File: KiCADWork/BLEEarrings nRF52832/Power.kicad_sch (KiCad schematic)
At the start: 17 parts, among them SW1 TK-6580B-1, U1 XB6096I2SV, U2 MCP73831T-2ACI/OT, U4 AP7361C-33FGE-7

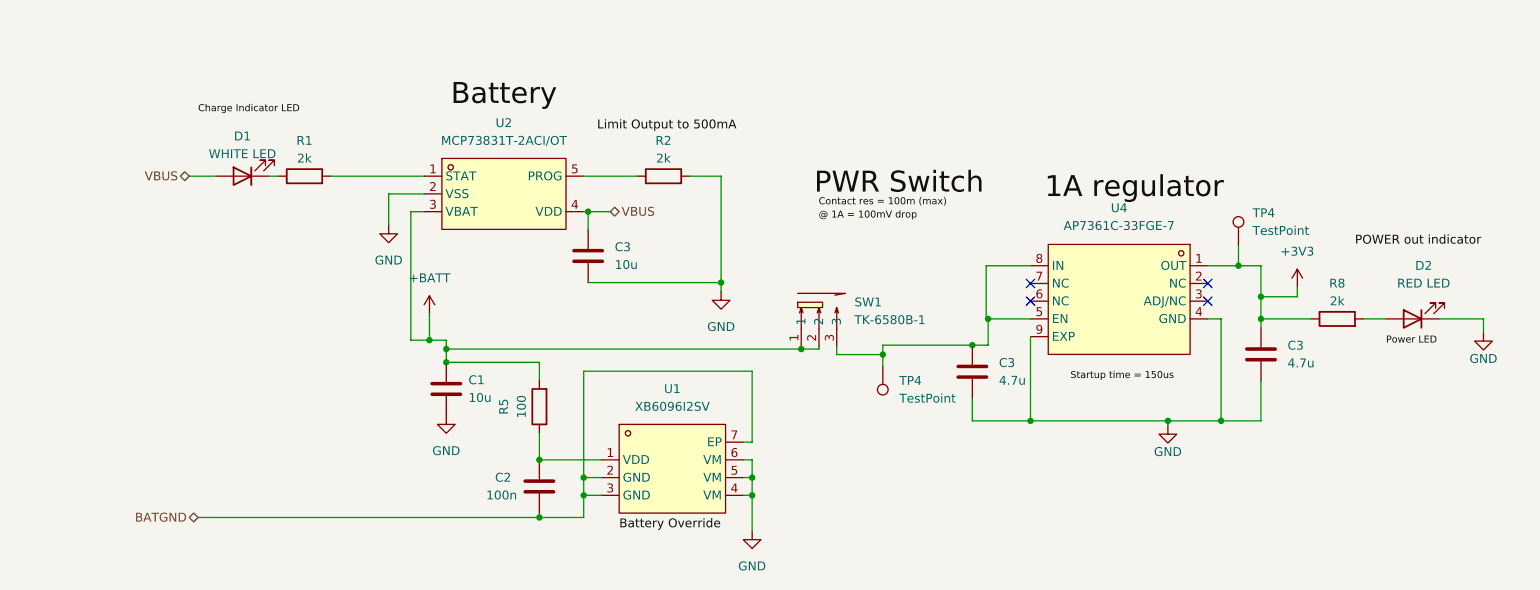
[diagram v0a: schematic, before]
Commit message: New Chip NRF52833
large changes
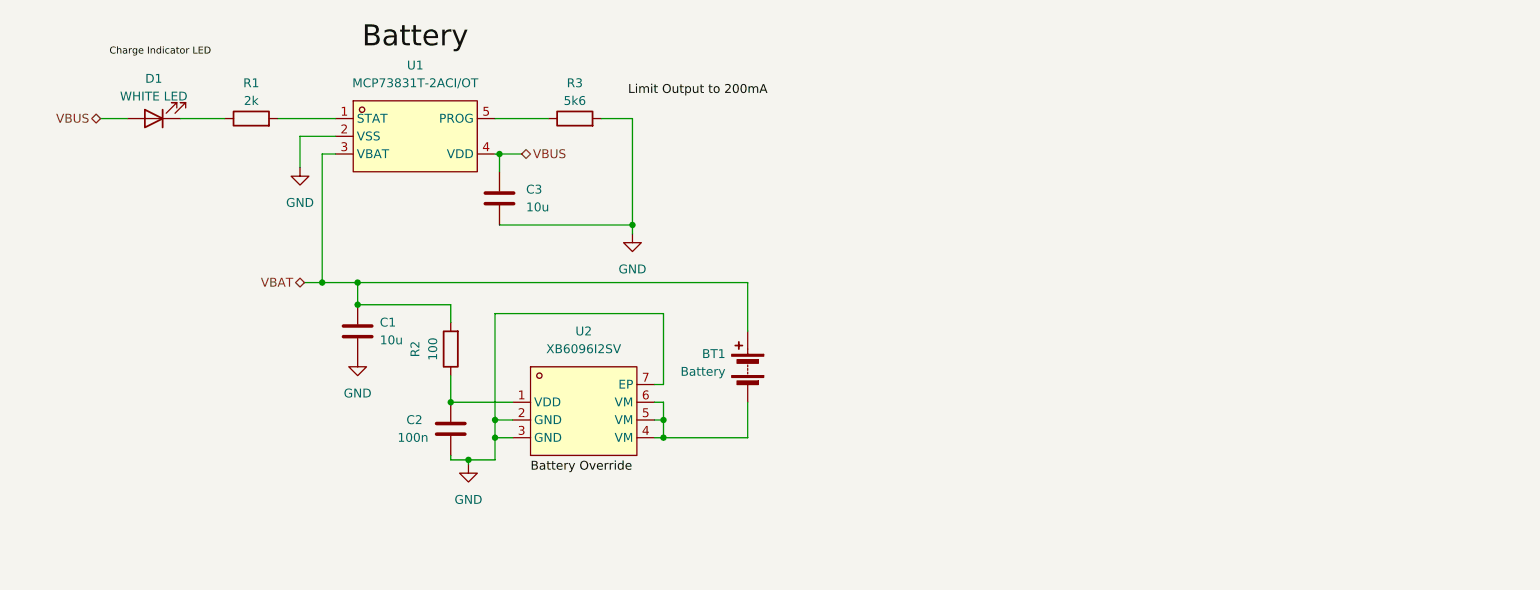
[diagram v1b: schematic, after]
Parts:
- removed C3 (x2): 4.7u, Capacitor_SMD:C_0402_1005Metric_Pad0.74x0.62mm_HandSolder, symbol Device:C
- removed C3: 10u, Capacitor_SMD:C_0402_1005Metric_Pad0.74x0.62mm_HandSolder, symbol Device:C
- removed D2: RED LED, LED_SMD:LED_0603_1608Metric_Pad1.05x0.95mm_HandSolder, symbol Device:LED
- removed R5: 100, Resistor_SMD:R_0402_1005Metric_Pad0.72x0.64mm_HandSolder, symbol Device:R
- removed R8: 2k, Resistor_SMD:R_0402_1005Metric_Pad0.72x0.64mm_HandSolder, symbol Device:R
- removed SW1: TK-6580B-1, easyeda2kicad:SW-TH_TK-6580B-1, symbol easyeda2kicad:TK-6580B-1
- removed TP4 (x2): TestPoint, TestPoint:TestPoint_Pad_D1.0mm, symbol Connector:TestPoint
- removed U1: XB6096I2SV, easyeda2kicad:WDFN-6_L2.0-W2.0-P0.65-BL-EP, symbol easyeda2kicad:XB6096I2SV
- removed U2: MCP73831T-2ACI/OT, easyeda2kicad:SOT-23-5_L3.0-W1.7-P0.95-LS2.8-BL, symbol easyeda2kicad:MCP73831T-2ACI_OT
- removed U4: AP7361C-33FGE-7, easyeda2kicad:DFN-8_L3.0-W3.0-P0.65-BL-EP, symbol easyeda2kicad:AP7361C-33FGE-7
- added BT1: Battery, easyeda2kicad:CONN-TH_1.25-2AW, symbol Device:Battery
- added C3: 10u, Capacitor_SMD:C_0402_1005Metric_Pad0.74x0.62mm_HandSolder, symbol Device:C
- added R3: 5k6, Resistor_SMD:R_0402_1005Metric_Pad0.72x0.64mm_HandSolder, symbol Device:R
- added U1: MCP73831T-2ACI/OT, easyeda2kicad:SOT-23-5_L3.0-W1.7-P0.95-LS2.8-BL, symbol easyeda2kicad:MCP73831T-2ACI_OT
- added U2: XB6096I2SV, easyeda2kicad:WDFN-6_L2.0-W2.0-P0.65-BL-EP, symbol easyeda2kicad:XB6096I2SV
- R2: value 2k -> 100
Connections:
- net BATGND is gone; now on net GND: C2.2
- net GND: now also C3.2, R3.2, U1.2 (VSS), U2.2 (GND), U2.3 (GND), U2.7 (EP); no longer R2.2
- net VBUS: now also C3.1, U1.4 (VDD)
- net at R2.1: now also C2.1, U2.1 (VDD)
- net at R1.2: now also U1.1 (STAT)
- net +BATT renamed VBAT
- net VBAT: now also R2.2, BT1.1 (+), U1.3 (VBAT)
- new net: R3.1, U1.5 (PROG)
- new net: BT1.2 (-), U2.4 (VM), U2.5 (VM), U2.6 (VM)
- no-connect marks 4 -> 0

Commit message: Dock Updates
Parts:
- R3: value 5k6 -> 4k99
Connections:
- net GND: now also U2.4 (VM), U2.5 (VM), U2.6 (VM); no longer U2.2 (GND), U2.3 (GND), U2.7 (EP)
- net VBAT: now also C2.1, U2.1 (VDD); no longer BT1.1 (+)
- new net: BT1.2 (-), U2.2 (GND), U2.3 (GND), U2.7 (EP)
- new net: BT1.1 (+), R2.1
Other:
- moved on the sheet: BT1

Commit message: Ignoring Backups
More Dock progress
All local backups removed
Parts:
- BT1: LCSC Part (none) -> C173752
- C1, C3: LCSC Part (none) -> C15525
- C2: LCSC Part (none) -> C60474
- D1: value WHITE LED -> RED LED; LCSC Part (none) -> C389517
- R1: LCSC Part (none) -> C60488
- R2: LCSC Part (none) -> C106233
- R3: LCSC Part (none) -> C137965
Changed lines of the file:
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@@
     (effects (font (size 3 3)) (justify left bottom))
   )
-  (label "Charge Indicator LED" (at 76.835 50.8 0) (fields_autoplaced)
+  (label "Charge Indicator LED" (at 76.835 51.435 0) (fields_autoplaced)
     (effects (font (size 1 1)) (justify left bottom))
   )
@@
     (effects (font (size 1.27 1.27)) (justify left bottom))
   )
-  (label "Go higher res value if need be (BUT NOT LOWER)" (at 147.955 58.42 0) (fields_autoplaced)
-    (effects (font (size 1.27 1.27)) (justify left bottom))
-  )
   (hierarchical_label "VBUS" (shape bidirectional) (at 135.89 64.77 0) (fields_autoplaced)
     (effects (font (size 1.27 1.27)) (justify left))
@@
       (effects (font (size 1.27 1.27)))
     )
-    (property "Value" "WHITE LED" (at 83.185 56.515 0)
+    (property "Value" "RED LED" (at 83.185 56.515 0)
       (effects (font (size 1.27 1.27)))
     )
@@
       (effects (font (size 1.27 1.27)) hide)
     )
+    (property "LCSC Part" "C389517 " (at 83.185 59.69 0)
+      (effects (font (size 1.27 1.27)) hide)
+    )
     (pin "1")
     (pin "2")
@@
     )
     (property "Datasheet" "~" (at 125.73 104.14 0)
+      (effects (font (size 1.27 1.27)) hide)
+    )
+    (property "LCSC Part" "C60474" (at 125.73 104.14 0)
       (effects (font (size 1.27 1.27)) hide)
     )
@@
       (effects (font (size 1.27 1.27)) hide)
     )
+    (property "LCSC Part" "C15525" (at 132.715 71.12 0)
+      (effects (font (size 1.27 1.27)) hide)
+    )
     (pin "1")
     (pin "2")
@@
     )
     (property "Datasheet" "~" (at 97.155 59.69 0)
+      (effects (font (size 1.27 1.27)) hide)
+    )
+    (property "LCSC Part" "C60488" (at 97.155 59.69 0)
       (effects (font (size 1.27 1.27)) hide)
     )
@@
       (effects (font (size 1.27 1.27)) hide)
     )
+    (property "LCSC Part" "C137965" (at 143.51 59.69 0)
+      (effects (font (size 1.27 1.27)) hide)
+    )
     (pin "1")
     (pin "2")
@@
       (effects (font (size 1.27 1.27)) hide)
     )
+    (property "LCSC Part" "C106233" (at 160.655 83.185 0)
+      (effects (font (size 1.27 1.27)) hide)
+    )
     (pin "1")
     (pin "2")
@@
       (effects (font (size 1.27 1.27)) hide)
     )
+    (property "LCSC Part" "C173752" (at 172.72 90.17 0)
+      (effects (font (size 1.27 1.27)) hide)
+    )
     (pin "1")
     (pin "2")
@@
       (effects (font (size 1.27 1.27)) hide)
     )
+    (property "LCSC Part" "C15525" (at 105.41 71.12 0)
+      (effects (font (size 1.27 1.27)) hide)
+    )

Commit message: Initial Dock DRC Complete
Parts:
- BT1: footprint easyeda2kicad:CONN-TH_1.25-2AW -> easyeda2kicad:CONN-TH_530480210; LCSC Part C173752 -> C505099
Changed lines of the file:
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@@
       (effects (font (size 1.27 1.27)) (justify left))
     )
-    (property "Footprint" "easyeda2kicad:CONN-TH_1.25-2AW" (at 172.72 88.646 90)
+    (property "Footprint" "easyeda2kicad:CONN-TH_530480210" (at 172.72 88.646 90)
       (effects (font (size 1.27 1.27)) hide)
     )
@@
       (effects (font (size 1.27 1.27)) hide)
     )
-    (property "LCSC Part" "C173752" (at 172.72 90.17 0)
+    (property "LCSC Part" "C505099" (at 172.72 90.17 0)
       (effects (font (size 1.27 1.27)) hide)
     )
